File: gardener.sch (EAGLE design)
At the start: 33 parts, among them IC2 REG1117

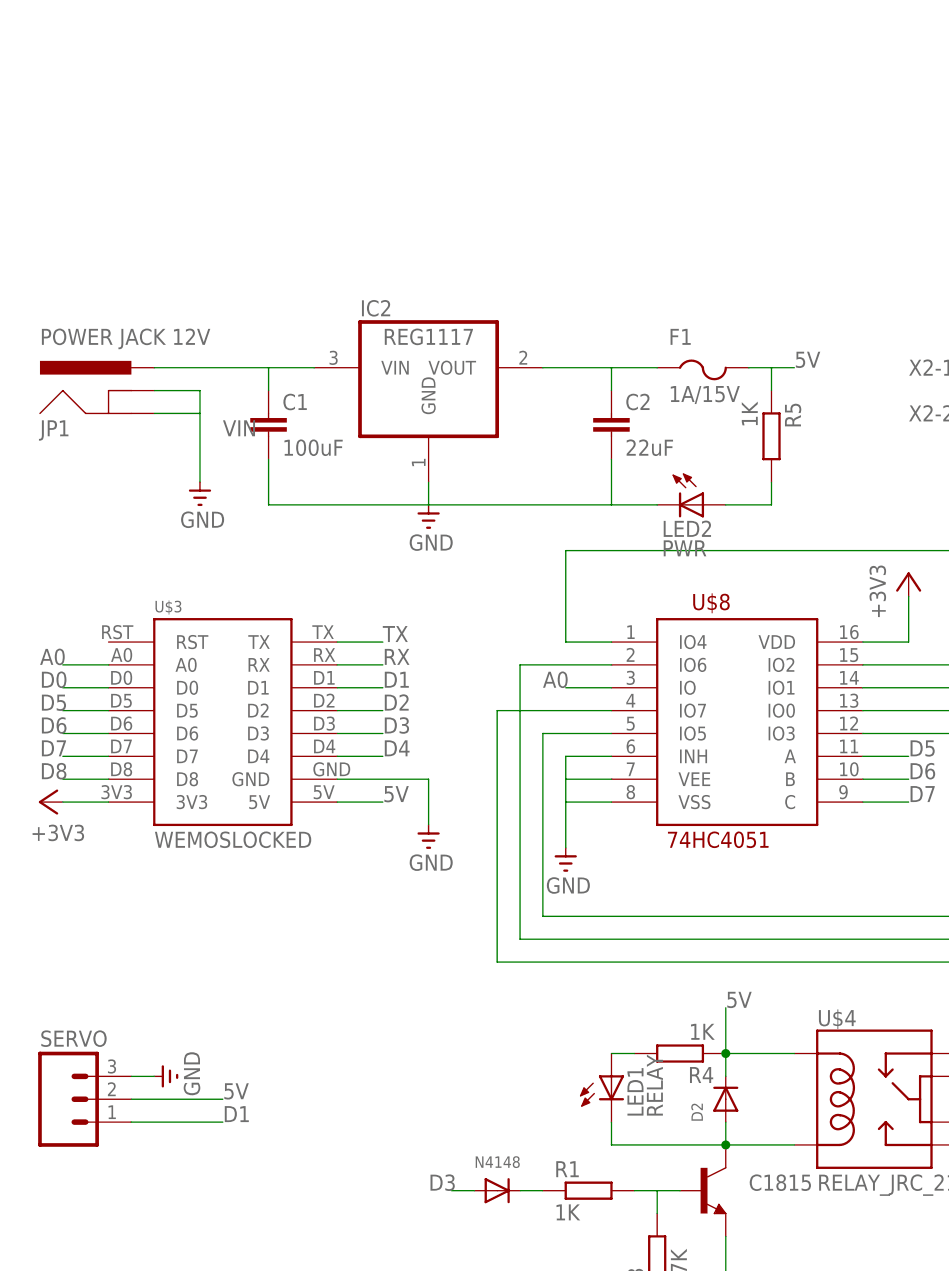
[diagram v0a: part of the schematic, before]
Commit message: Update design to add one more AMS1117 for servo
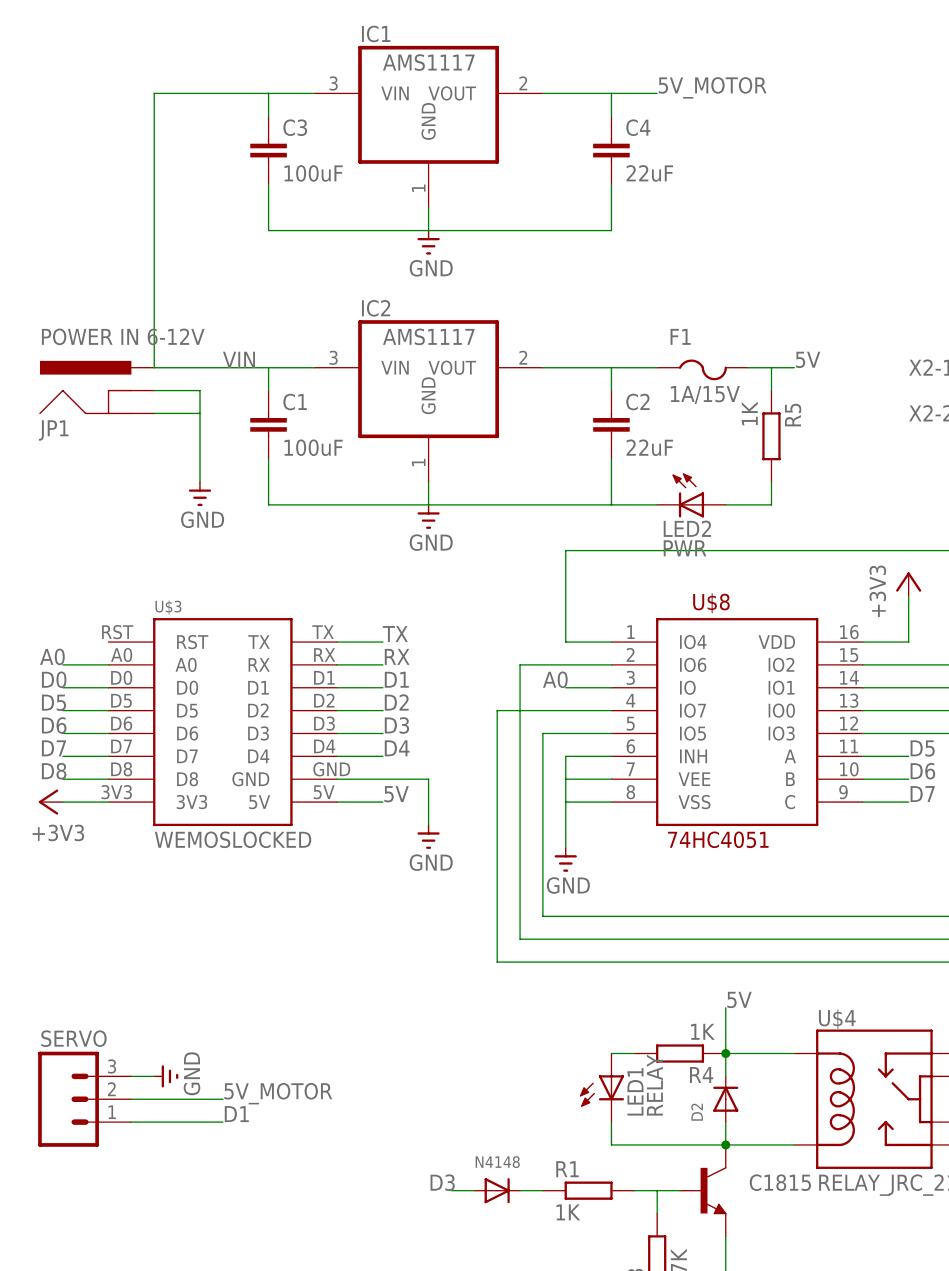
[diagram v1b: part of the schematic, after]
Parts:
- added C3: 100uF, rcl:C-EUC0805
- added C4: 22uF, rcl:C-EUC0805
- added IC1: AMS1117, burr-brown:REG1117
- IC2: value REG1117 -> AMS1117
- JP1: value POWER JACK 12V -> POWER IN 6-12V
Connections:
- new net 5V_MOTOR: C4.1, IC1.VOUT, SERVO.2
- net 5V: no longer SERVO.2
- net GND: now also C3.2, C4.2, IC1.GND
- net VIN: now also C3.1, IC1.VIN

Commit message: Update design to version 0.2
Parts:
- removed C1, C3: 100uF, rcl:C-EUC0805
- removed C2, C4: 22uF, rcl:C-EUC0805
- removed DHT22: (no value), RHT03_DHT-22_AM2302:RHT03_DHT-22_AM2302WIRED
- removed F1: 1A/15V, adafruit:PTCFUSE-1812
- removed IC1, IC2: AMS1117, burr-brown:REG1117
- removed JP1: POWER IN 6-12V, SparkFun-Connectors:POWER_JACKPTH
- removed R2: 10K, rcl:R-EU_R0805
- removed S2: SWITCH-MOMENTARY-212MM, SparkFun-Electromechanical:SWITCH-MOMENTARY-212MM
- removed U$4: RELAY_JRC_21F, My Eagle Lib:MINIATURE_RELAY_JRC_21F
- removed X4: (no value), con-wago-500:W237-102
- added C5, C6: 100uF/35V, SparkFun-Passives:CAP_POLD
- added CAP_BTN: (no value), SparkFun-Connectors:M03PTH
- added D3: SS34, SparkFun-DiscreteSemi:MBRA140
- added IC4: LM2596S, national-semiconductor:LM2596S
- added JP2: POWER IN, SparkFun-Connectors:POWER_JACKPTH
- added L3: 100uH, SparkFun-Passives:INDUCTORSDR13-7-270ML
- added OLED: (no value), SparkFun-Connectors:M04PTH
- added RELAY: ZNS5106, relay:ZNS5106
- added SW_BTN: SWITCH-MOMENTARY-212MM, SparkFun-Electromechanical:SWITCH-MOMENTARY-212MM
- added WAKE: (no value), SparkFun-Connectors:M02PTH
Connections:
- removed net 5V_MOTOR: C4.1, IC1.VOUT, SERVO.2
- removed net VOUT: C2.1, F1.1, IC2.VOUT
- new net N$9: D3.C, IC4.OUT, L3.1
- new net RST: U$3.RST, WAKE.1
- net +3V3: now also CAP_BTN.3, OLED.1, SW_BTN.2; no longer DHT22.VDD, R2.1, X4-1.KL
- net 5V: now also C6.+, IC4.FB, L3.2, RELAY1.1, SERVO.2; no longer F1.2, U$4.COIL1
- net COM: now also RELAY2.P; no longer U$4.COM1, U$4.COM2
- net D0: now also WAKE.2
- net D2: now also N4148.A
- net D3: now also OLED.3; no longer N4148.A
- net D4: now also OLED.4; no longer S2.1
- net D8: now also CAP_BTN.2, SW_BTN.1; no longer DHT22.DATA, R2.2
- net GND: now also C5.-, C6.-, CAP_BTN.1, D3.A, IC4.!ON!/OFF, IC4.GND, JP2.GND, JP2.GNDBREAK, OLED.2; no longer C1.2, C2.2, C3.2, C4.2, DHT22.GND, IC1.GND, IC2.GND, JP1.GND, JP1.GNDBREAK, S2.2, X4-2.KL
- net N$1: now also RELAY1.2; no longer U$4.COIL2
- net NC: now also RELAY2.O; no longer U$4.NC
- net NO: now also RELAY2.S; no longer U$4.NO
- net VIN: now also C5.+, IC4.VIN, JP2.PWR; no longer C1.1, C3.1, IC1.VIN, IC2.VIN, JP1.PWR
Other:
- moved on the sheet: A1, A2, A3, A4, A5, A6, A7, A8, C1815, D2, LED1, LED2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
